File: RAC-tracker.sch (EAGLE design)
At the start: 27 parts, among them J1 U.FL, J2 U.FL, U2 SIM-ST-MFF2, U3 MCP73831

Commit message: Added GPS frontend, further integrated NRF9160
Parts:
- added C10, C11: 4.7uF, SparkFun-Capacitors:4.7UF0603
- added C12: 1nF, SparkFun-Capacitors:1.0NF/1000PF-0603-50V-10%
- added J5, J6: U.FL, SparkFun-Connectors:U.FL
- added L1: 10nH, rocket-components:LQW18AS10NG00D
- added R3: 10k, SparkFun-Resistors:10KOHM-0603-1/10W-1%
- added R4: 1M, SparkFun-Resistors:1MOHM-0603-1/4W-5%
- added U4: NRF9160-SICA-R, rocket-components:NRF9160-SICA-R
- added U5: (no value), rocket-components:NJG1156PCD
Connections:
- new net 3.3V: C11.1, C12.1, U4.VDD_GPIO, U5.VDD
- new net GPS_ANT: J5.SIGNAL, U5.PRE_IN
- new net GPS_EN: R4.2, U4.MAGPIO0, U5.VCTL
- new net GPS_RF: U4.GPS, U5.POST_OUT
- new net N$1: R3.1, U4.ENABLE
- new net N$2: J6.SIGNAL, U4.ANT
- new net N$3: L1.2, U5.PRE_OUT
- new net N$4: L1.1, U5.LNA_IN
- net GND: now also C10.2, C11.2, C12.2, J5.GND@0, J5.GND@1, J6.GND@0, J6.GND@1, R4.1, U4.GND_SHIELD, U4.VSS, U5.EP, U5.GND, U5.GND@1, U5.GND@2, U5.GND@3
- net SIM_CLK: now also U4.SIM_CLK
- net SIM_DATA: now also U4.SIM_IO
- net SIM_RST: now also U4.SIM_RST
- net SIM_VIN: now also U4.SIM_1V8
- net V_BATT: now also C10.1, R3.2, U4.VDD

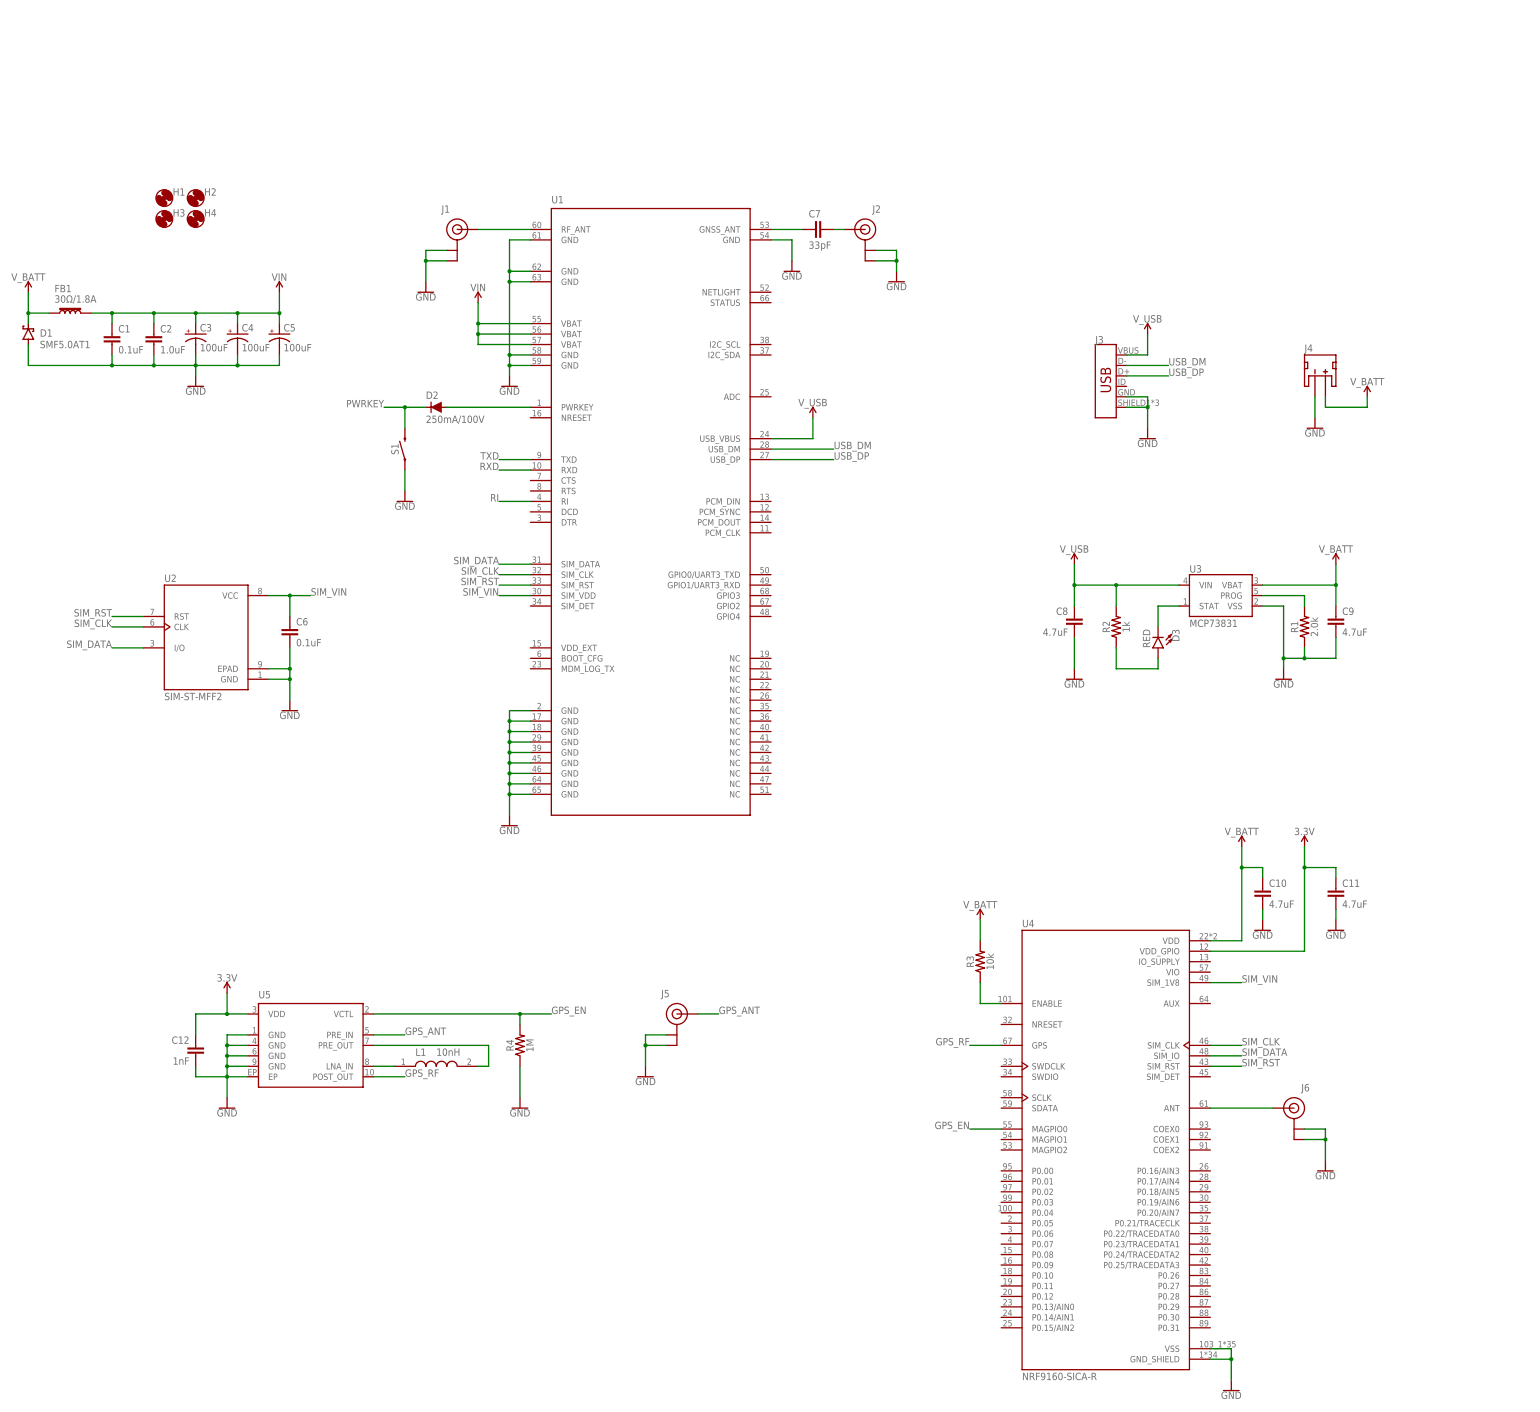
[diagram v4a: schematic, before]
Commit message: Replaced GPS front-end, added 1.8V LDO
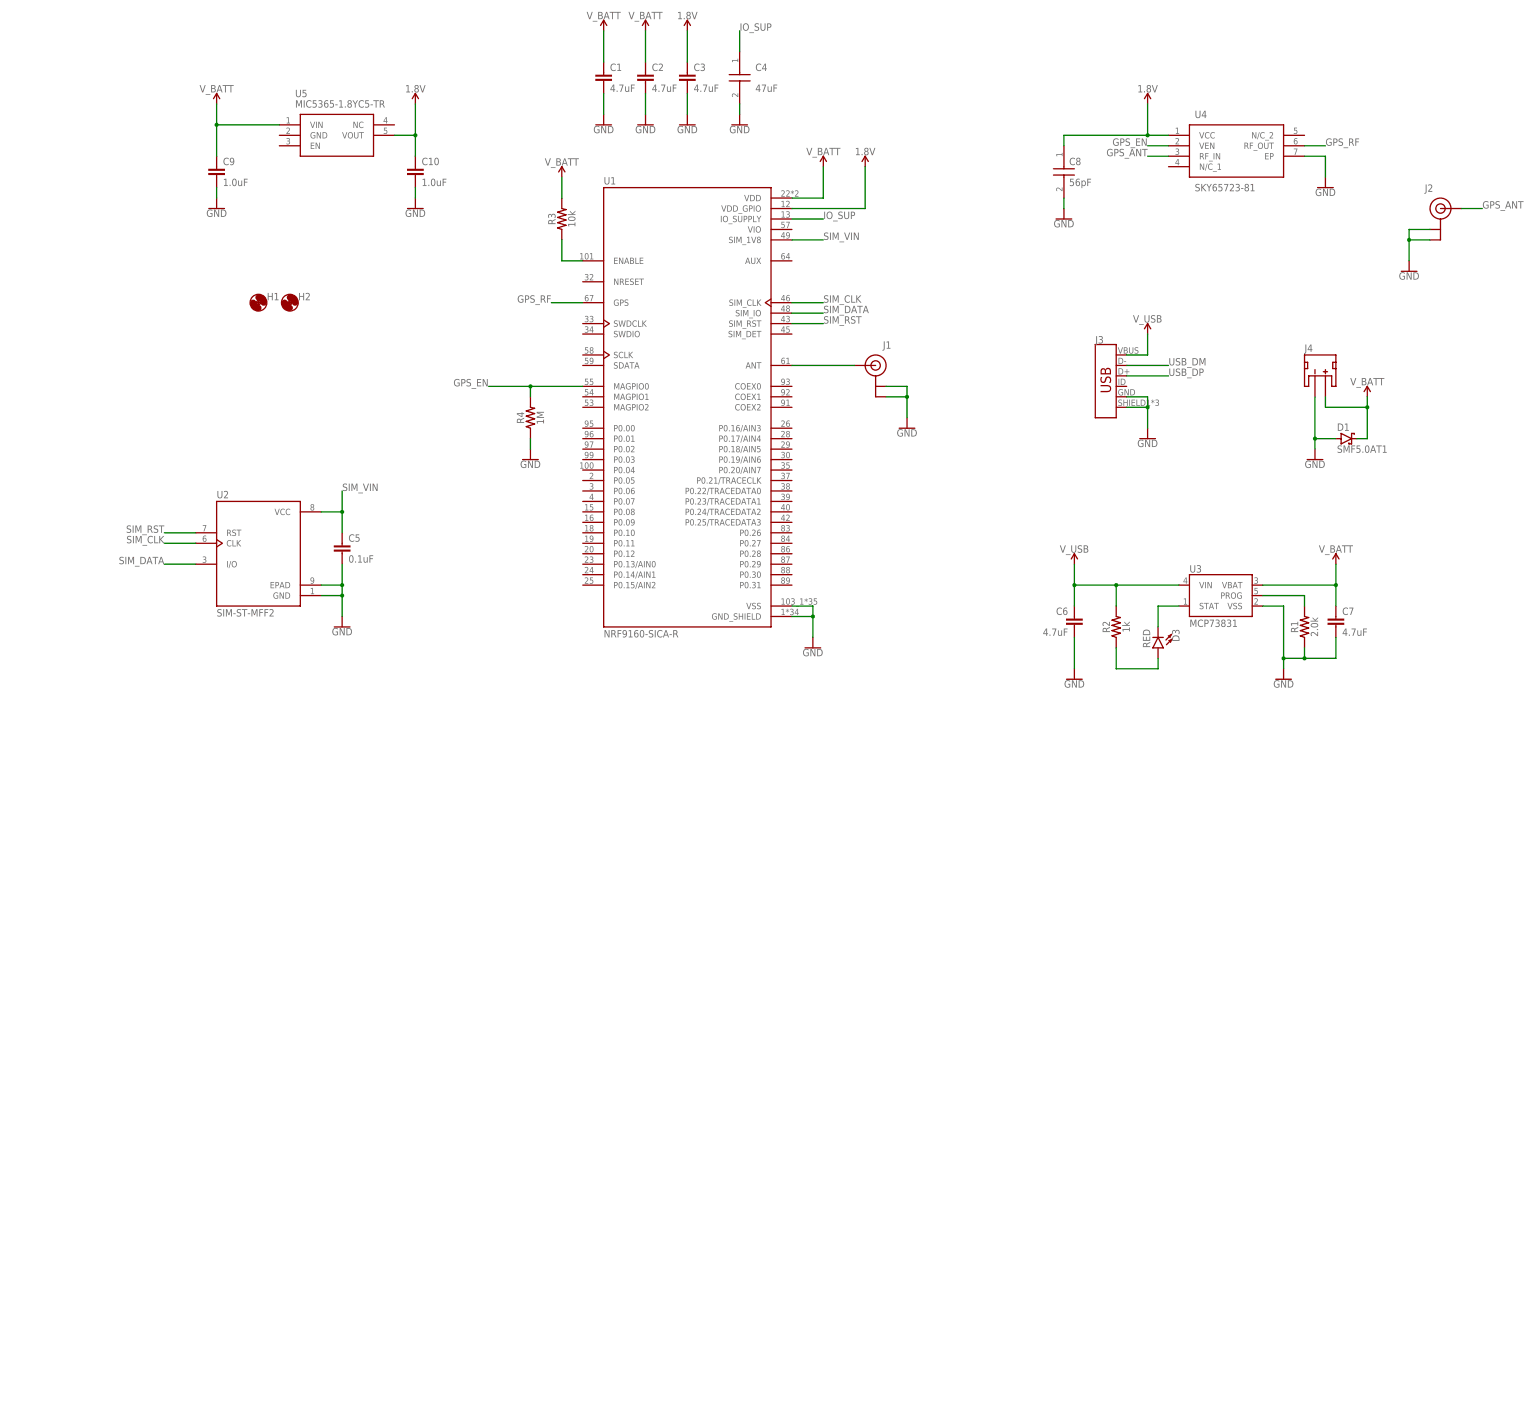
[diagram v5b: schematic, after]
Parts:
- removed C11: 4.7uF, SparkFun-Capacitors:4.7UF0603
- removed C12: 1nF, SparkFun-Capacitors:1.0NF/1000PF-0603-50V-10%
- removed D2: 250mA/100V, SparkFun-DiscreteSemi:DIODE-BAS16J
- removed FB1: 30Ω/1.8A, SparkFun-Coils:FERRITE_BEAD-0603
- removed H3, H4: MOUNT-HOLE2.8, holes:MOUNT-HOLE2.8
- removed J5, J6: U.FL, SparkFun-Connectors:U.FL
- removed L1: 10nH, rocket-components:LQW18AS10NG00D
- removed S1: MOMENTARY-SWITCH-SPST-SMD-5.2MM, SparkFun-Switches:MOMENTARY-SWITCH-SPST-SMD-5.2MM
- C1, C6: value 0.1uF -> 4.7uF; device SparkFun-Capacitors:0.1UF-0603-25V-(+80/-20%) -> SparkFun-Capacitors:4.7UF0603
- C10, C9: value 4.7uF -> 1.0uF; device SparkFun-Capacitors:4.7UF0603 -> SparkFun-Capacitors:1.0UF-0603-16V-10%
- C2: value 1.0uF -> 4.7uF; device SparkFun-Capacitors:1.0UF-0603-16V-10% -> SparkFun-Capacitors:4.7UF0603
- C3: value 100uF -> 4.7uF; device SparkFun-Capacitors:100UF-POLAR-EIA7343-10V-10%(TANT) -> SparkFun-Capacitors:4.7UF0603
- C4: value 100uF -> 47uF; device SparkFun-Capacitors:100UF-POLAR-EIA7343-10V-10%(TANT) -> rocket-components:JMK212BBJ476MG-T
- C5: value 100uF -> 0.1uF; device SparkFun-Capacitors:100UF-POLAR-EIA7343-10V-10%(TANT) -> SparkFun-Capacitors:0.1UF-0603-25V-(+80/-20%)
- C7: value 33pF -> 4.7uF; device SparkFun-Capacitors:33PF-0603-50V-5% -> SparkFun-Capacitors:4.7UF0603
- C8: value 4.7uF -> 56pF; device SparkFun-Capacitors:4.7UF0603 -> rocket-components:GRM1885C1H560JA01J
- U1: value (none) -> NRF9160-SICA-R; device rocket-components:SIM7000 -> rocket-components:NRF9160-SICA-R
- U4: value NRF9160-SICA-R -> SKY65723-81; device rocket-components:NRF9160-SICA-R -> rocket-components:SKY65723-81
- U5: value (none) -> MIC5365-1.8YC5-TR; device rocket-components:NJG1156PCD -> rocket-components:MIC5365-1.8YC5-TR
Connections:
- removed net 3.3V: C11.1, C12.1, U4.VDD_GPIO, U5.VDD
- removed net GNSS_OUT: C7.2, J2.SIGNAL
- removed net GNSS_RF: C7.1, U1.GNSS_ANT
- removed net LTE_OUT: J1.SIGNAL, U1.RF_ANT
- removed net N$1: R3.1, U4.ENABLE
- removed net N$2: J6.SIGNAL, U4.ANT
- removed net N$3: L1.2, U5.PRE_OUT
- removed net N$4: L1.1, U5.LNA_IN
- removed net PWRKEY: D2.C, S1.2
- removed net PWRKEY_AN: D2.A, U1.PWRKEY
- removed net RI: U1.RI
- removed net RXD: U1.RXD
- removed net TXD: U1.TXD
- removed net VIN: C1.1, C2.1, C3.+, C4.+, C5.+, FB1.2, U1.VBAT, U1.VBAT@1, U1.VBAT@2
- new net 1.8V: C10.1, C3.1, C8.1, U1.VDD_GPIO, U4.VCC, U5.VOUT
- new net EN: R3.1, U1.ENABLE
- new net IO_SUP: C4.1, U1.IO_SUPPLY
- new net LTE_ANT: J1.SIGNAL, U1.ANT
- net GND: now also C3.2, C4.2, C5.2, C7.2, U1.GND_SHIELD, U1.VSS, U4.EP; no longer C11.2, C12.2, C3.-, C4.-, C5.-, J5.GND@0, J5.GND@1, J6.GND@0, J6.GND@1, S1.1, U1.GND, U1.GND@1, U1.GND@10, U1.GND@11, U1.GND@12, U1.GND@13, U1.GND@14, U1.GND@2, U1.GND@3, U1.GND@4, U1.GND@5, U1.GND@6, U1.GND@7, U1.GND@8, U1.GND@9, U4.GND_SHIELD, U4.VSS, U5.EP, U5.GND, U5.GND@1, U5.GND@2, U5.GND@3
- net GPS_ANT: now also J2.SIGNAL, U4.RF_IN; no longer J5.SIGNAL, U5.PRE_IN
- net GPS_EN: now also U1.MAGPIO0, U4.VEN; no longer U4.MAGPIO0, U5.VCTL
- net GPS_RF: now also U1.GPS, U4.RF_OUT; no longer U4.GPS, U5.POST_OUT
- net SIM_CLK: no longer U4.SIM_CLK
- net SIM_DATA: now also U1.SIM_IO; no longer U1.SIM_DATA, U4.SIM_IO
- net SIM_RST: no longer U4.SIM_RST
- net SIM_VIN: now also C5.1, U1.SIM_1V8; no longer C6.1, U1.SIM_VDD, U4.SIM_1V8
- net USB_DM: no longer U1.USB_DM
- net USB_DP: no longer U1.USB_DP
- net V_BATT: now also C1.1, C2.1, C7.1, U1.VDD, U5.VIN; no longer C10.1, FB1.1, U4.VDD
- net V_USB: now also C6.1; no longer C8.1, U1.USB_VBUS
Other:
- moved on the sheet: C1, C10, C2, C4, C6, C7, C9, D1, H1, H2, J1, J2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

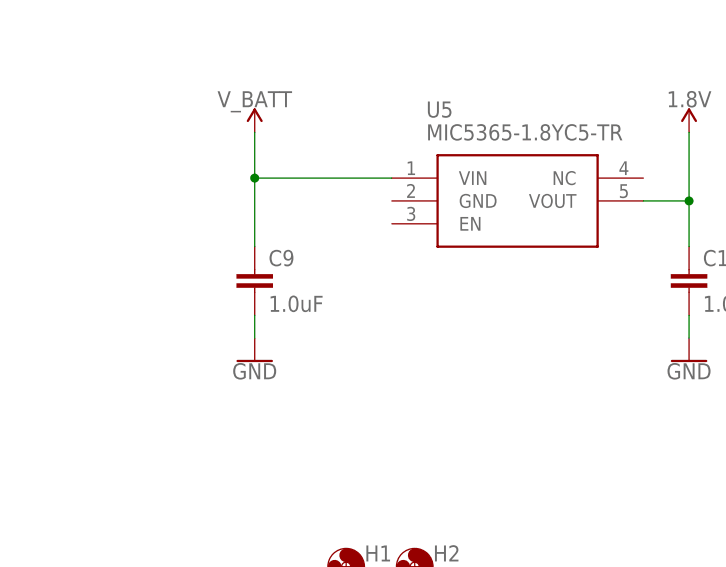
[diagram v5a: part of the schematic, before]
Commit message: Fixed missing LDO nets, started routing board
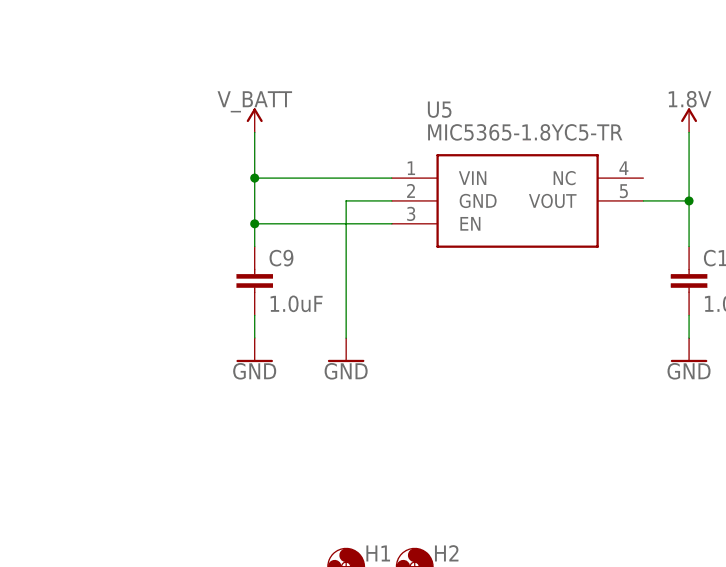
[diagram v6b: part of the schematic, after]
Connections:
- net GND: now also U5.GND
- net V_BATT: now also U5.EN
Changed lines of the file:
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@@
 <part name="SUPPLY15" library="SparkFun-PowerSymbols" library_urn="urn:adsk.eagle:library:530" deviceset="1.8V" device=""/>
 <part name="SUPPLY16" library="SparkFun-PowerSymbols" library_urn="urn:adsk.eagle:library:530" deviceset="1.8V" device=""/>
+<part name="GND18" library="SparkFun-PowerSymbols" library_urn="urn:adsk.eagle:library:530" deviceset="GND" device=""/>
 </parts>
 <sheets>
@@
 <instance part="SUPPLY16" gate="G$1" x="175.26" y="81.28" smashed="yes">
 <attribute name="VALUE" x="175.26" y="84.074" size="1.778" layer="96" align="bottom-center"/>
+</instance>
+<instance part="GND18" gate="1" x="-40.64" y="55.88" smashed="yes">
+<attribute name="VALUE" x="-40.64" y="55.626" size="1.778" layer="96" align="top-center"/>
 </instance>
 </instances>
@@
 <wire x1="-50.8" y1="58.42" x2="-50.8" y2="60.96" width="0.1524" layer="91"/>
 </segment>
+<segment>
+<pinref part="GND18" gate="1" pin="GND"/>
+<wire x1="-40.64" y1="58.42" x2="-40.64" y2="73.66" width="0.1524" layer="91"/>
+<pinref part="U5" gate="G$1" pin="GND"/>
+<wire x1="-40.64" y1="73.66" x2="-35.56" y2="73.66" width="0.1524" layer="91"/>
+</segment>
 </net>
 <net name="SIM_VIN" class="0">
@@
 <wire x1="-35.56" y1="76.2" x2="-50.8" y2="76.2" width="0.1524" layer="91"/>
 <pinref part="C9" gate="G$1" pin="1"/>
-<wire x1="-50.8" y1="76.2" x2="-50.8" y2="68.58" width="0.1524" layer="91"/>
+<wire x1="-50.8" y1="76.2" x2="-50.8" y2="71.12" width="0.1524" layer="91"/>
+<wire x1="-50.8" y1="71.12" x2="-50.8" y2="68.58" width="0.1524" layer="91"/>
 <wire x1="-50.8" y1="76.2" x2="-50.8" y2="81.28" width="0.1524" layer="91"/>
 <junction x="-50.8" y="76.2"/>
 <pinref part="SUPPLY12" gate="G$1" pin="V_BATT"/>
-</segment>
-</net>
+<pinref part="U5" gate="G$1" pin="EN"/>
+<wire x1="-35.56" y1="71.12" x2="-50.8" y2="71.12" width="0.1524" layer="91"/>
+<junction x="-50.8" y="71.12"/>
+</segment>
+</net>
